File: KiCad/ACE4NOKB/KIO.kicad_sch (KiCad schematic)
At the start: 6 parts, among them J1 Conn_02x06_Odd_Even, J300 Conn_02x06_Odd_Even, J301 Conn_02x06_Odd_Even, J303 Conn_02x06_Odd_Even, J305 Conn_02x05_Odd_Even

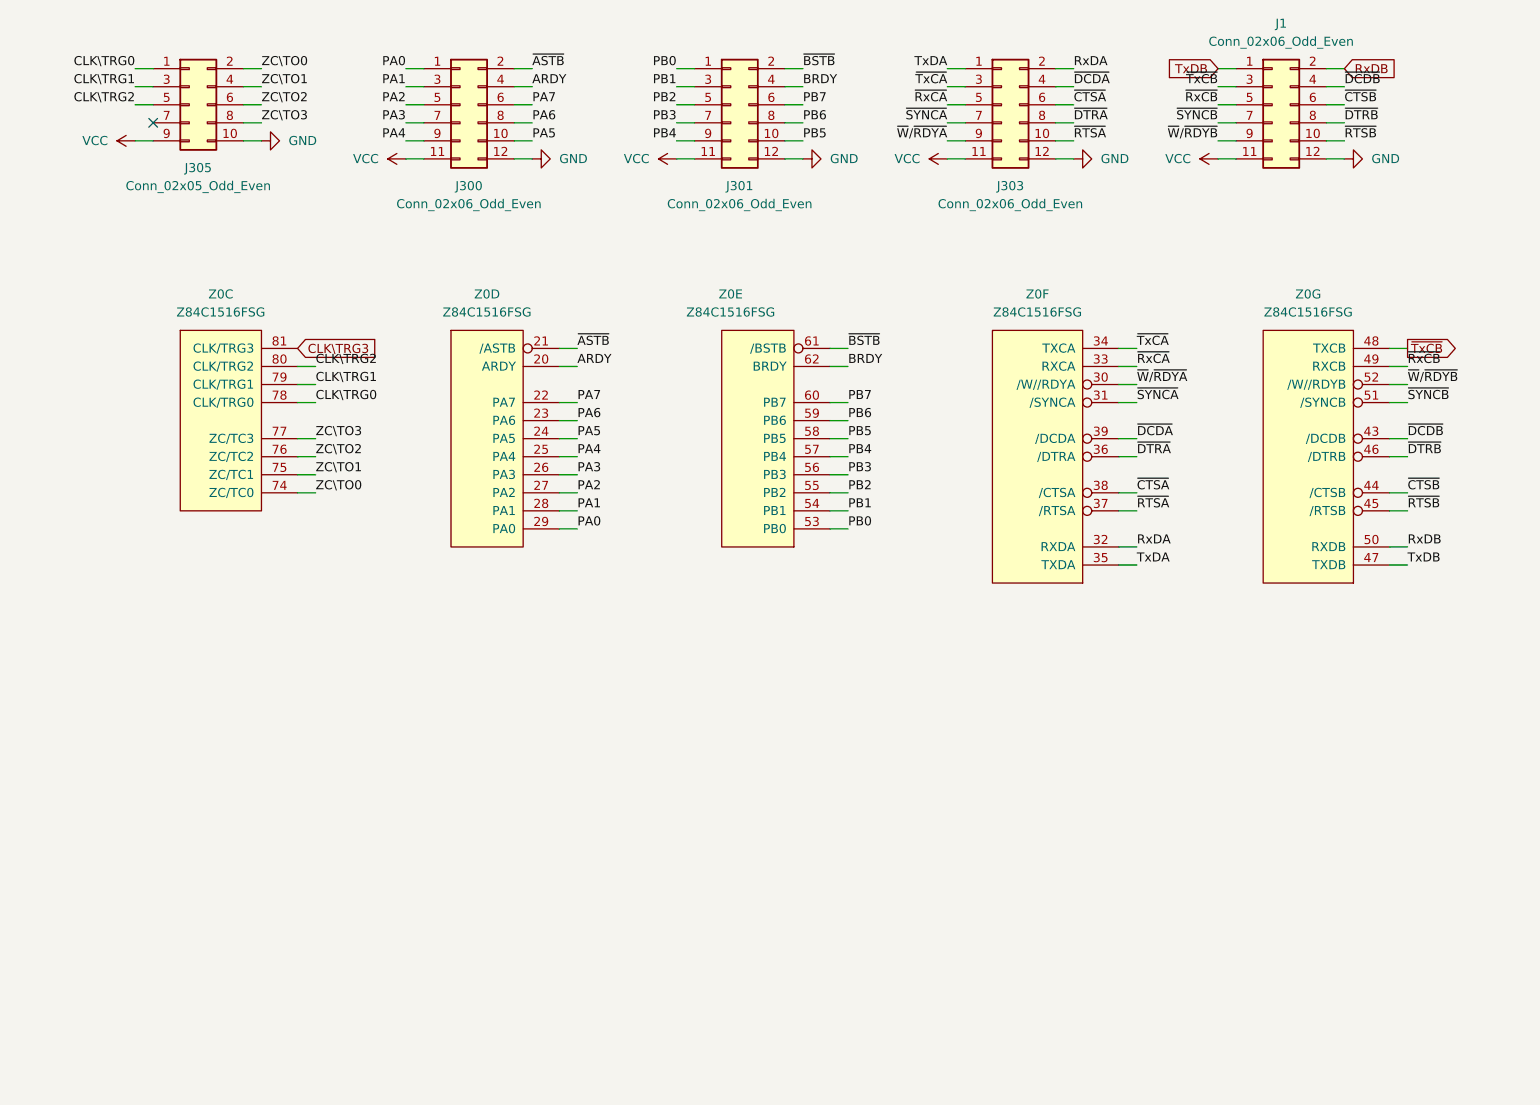
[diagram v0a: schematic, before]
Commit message: Fix mistake with ROM Select.
Signed-off-by: John Bradley <flypie@rocketmail.com>
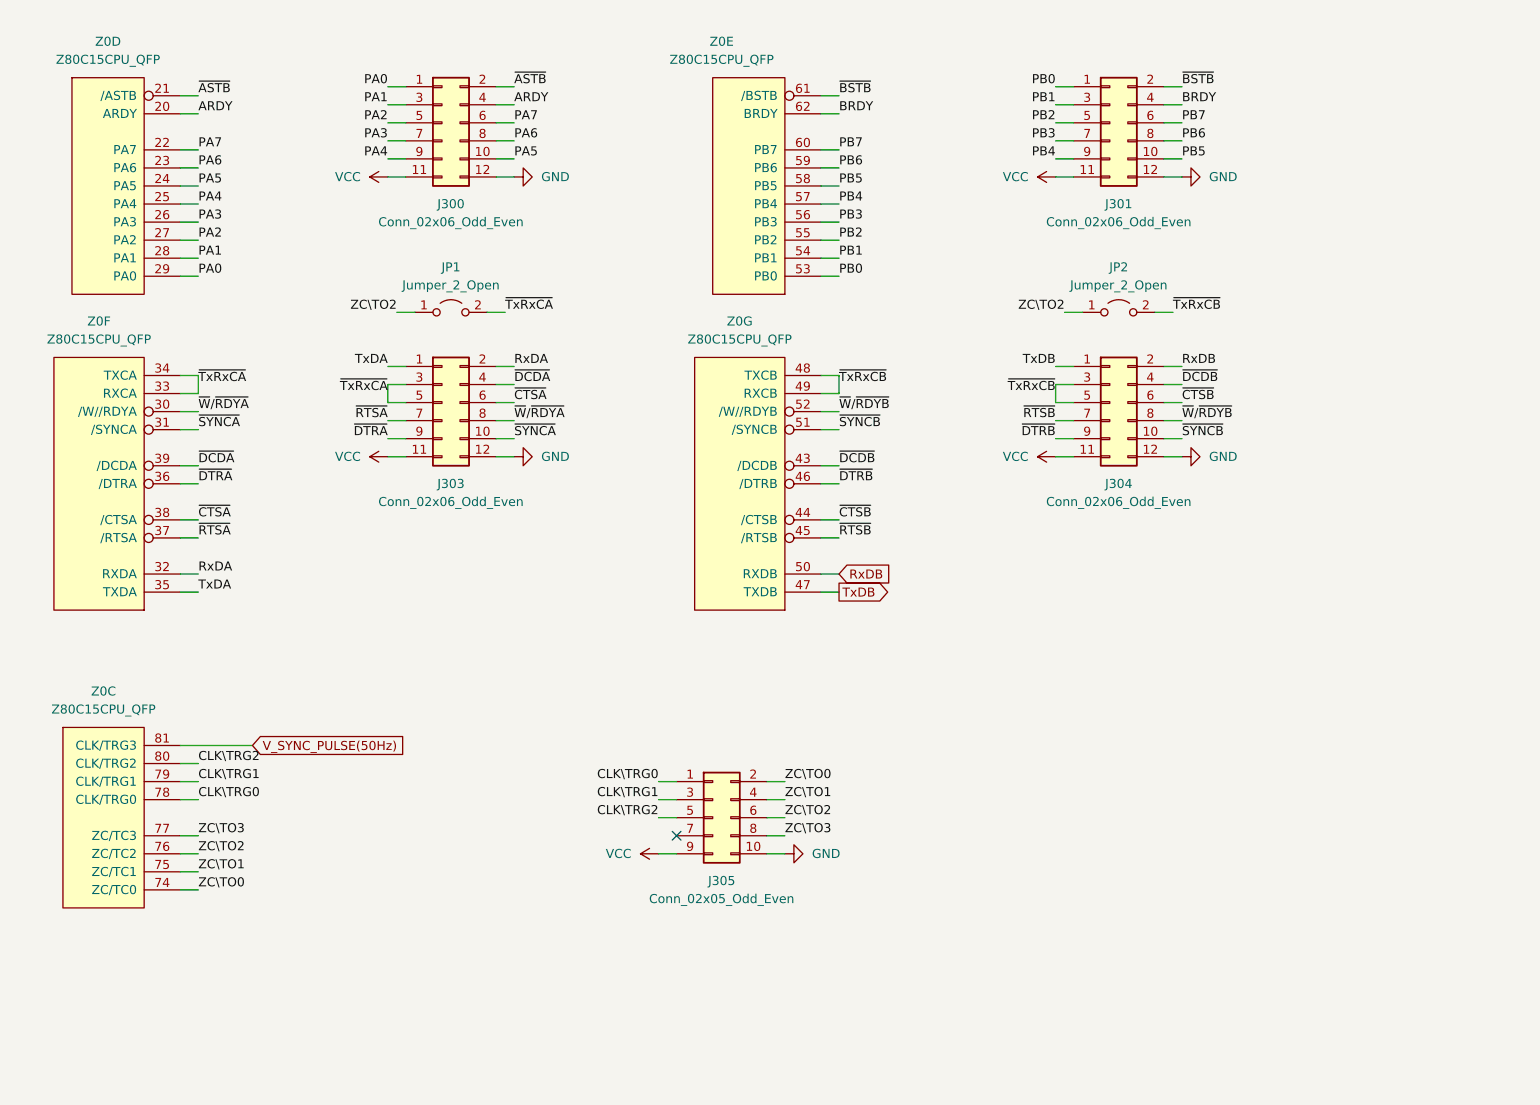
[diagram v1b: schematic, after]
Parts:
- removed J1: Conn_02x06_Odd_Even, Connector_PinHeader_2.54mm:PinHeader_2x06_P2.54mm_Vertical, symbol Connector_Generic:Conn_02x06_Odd_Even
- added J304: Conn_02x06_Odd_Even, Connector_PinHeader_2.54mm:PinHeader_2x06_P2.54mm_Vertical, symbol Connector_Generic:Conn_02x06_Odd_Even
- added JP1, JP2: Jumper_2_Open, Connector_PinHeader_2.54mm:PinHeader_1x02_P2.54mm_Vertical, symbol Jumper:Jumper_2_Open
- J300, J301: Manufacturer_Name Amphenol FCI -> SAMTEC; Manufacturer_Part_Number 10129381-912003BLF -> HTSW-106-08-S-D
- J303: Manufacturer_Name Amphenol FCI -> SAMTEC; Manufacturer_Part_Number 10129381-908002BLF -> TSW-104-08-S-D
- J305: Manufacturer_Name Amphenol FCI -> TE Connectivity / AMP; Manufacturer_Part_Number 10129381-910001BLF -> HTSW-105-08-S-D
- Z0: value Z84C1516FSG -> Z80C15CPU_QFP
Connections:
- net ~{TxCA} is gone; now on net ~{TxRxCA}: J303.3 (Pin_3), Z0.34 (TXCA)
- net ~{TxCB} is gone; now on net ~{TxRxCB}: Z0.48 (TXCB)
- net GND: now also J304.12 (Pin_12)
- net RxDB: now also J304.2 (Pin_2)
- net TxDB: now also J304.1 (Pin_1)
- net VCC: now also J304.11 (Pin_11)
- net ZC\TO2: now also JP1.1 (A), JP2.1 (A)
- net ~{CTSB}: now also J304.6 (Pin_6)
- net ~{DCDB}: now also J304.4 (Pin_4)
- net ~{DTRA}: now also J303.9 (Pin_9); no longer J303.8 (Pin_8)
- net ~{DTRB}: now also J304.9 (Pin_9)
- net ~{RTSA}: now also J303.7 (Pin_7); no longer J303.10 (Pin_10)
- net ~{RTSB}: now also J304.7 (Pin_7)
- net ~{SYNCA}: now also J303.10 (Pin_10); no longer J303.7 (Pin_7)
- net ~{SYNCB}: now also J304.10 (Pin_10)
- net ~{W}/~{RDYA}: now also J303.8 (Pin_8); no longer J303.9 (Pin_9)
- net ~{W}/~{RDYB}: now also J304.8 (Pin_8)
- net CLK\TRG3 renamed V_SYNC_PULSE(50Hz)
- net ~{RxCA} renamed ~{TxRxCA}
- net ~{TxRxCA}: now also JP1.2 (B)
- net ~{RxCB} renamed ~{TxRxCB}
- net ~{TxRxCB}: now also J304.3 (Pin_3), J304.5 (Pin_5), JP2.2 (B)
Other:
- moved on the sheet: J300, J301, J303, J305

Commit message: Update to last expermintal version. Uses clock sythsiser and can be switched between full ACE compatible and inhanced IO. Should be able to switch between multiple ROM images tosred on the same chip.
Signed-off-by: John Bradley <flypie@rocketmail.com>
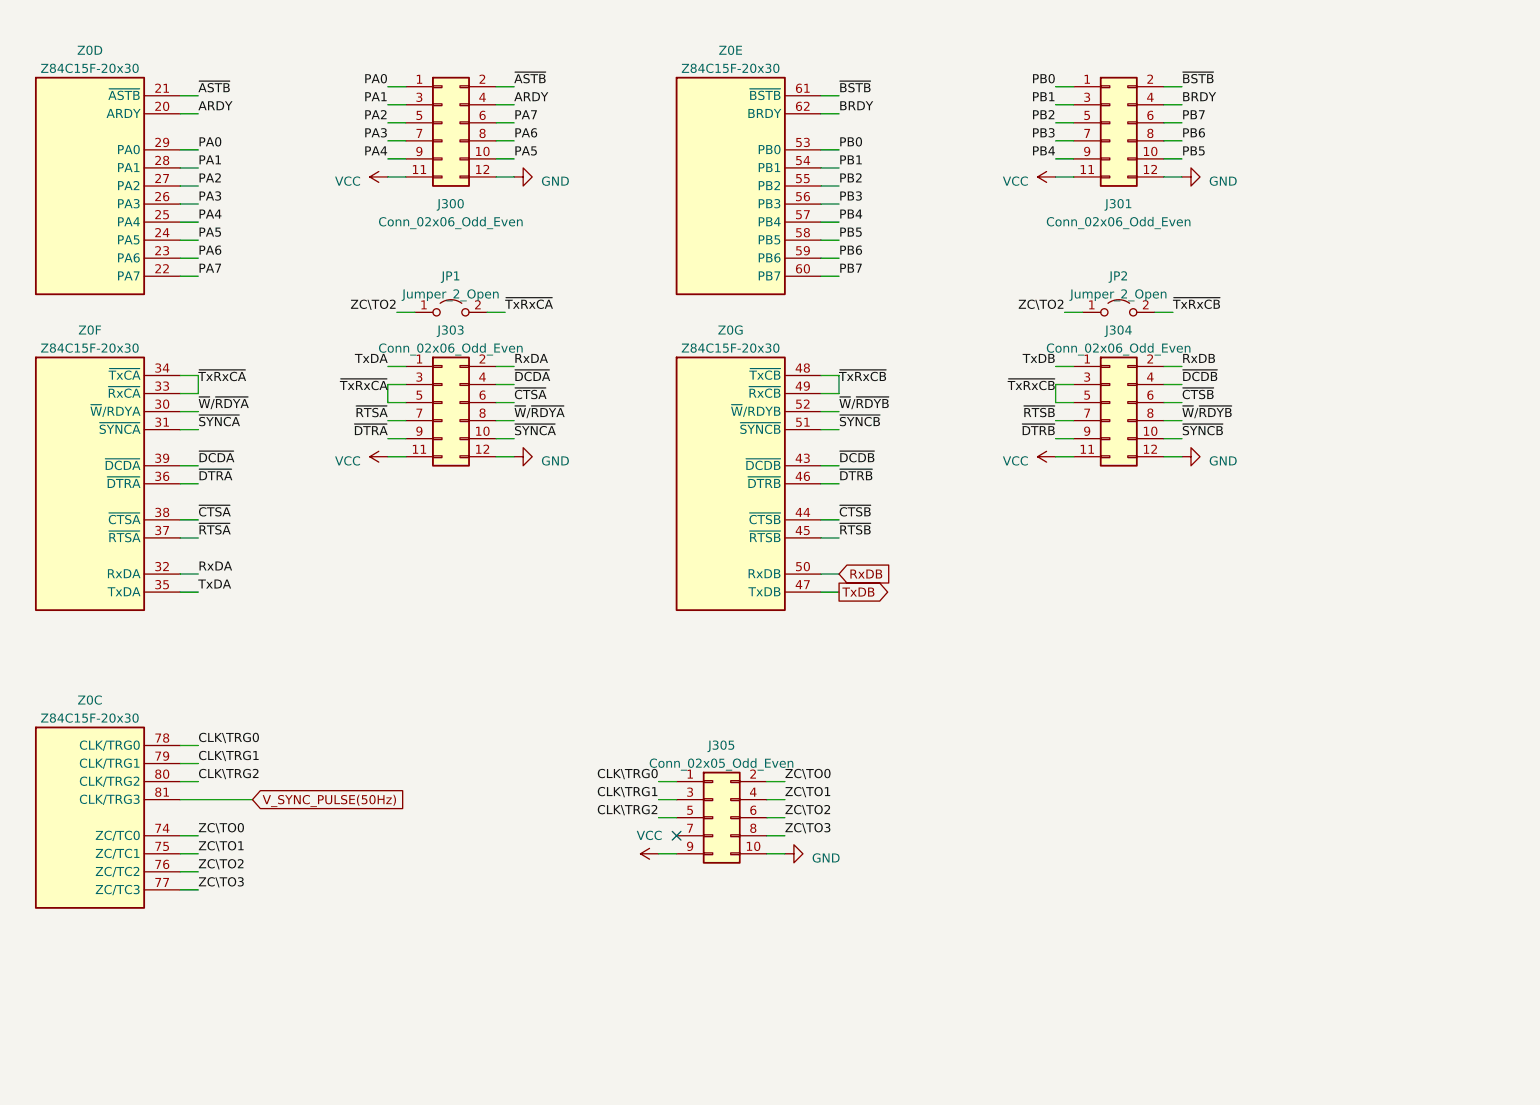
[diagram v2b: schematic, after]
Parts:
- J300, J301: Manufacturer_Name SAMTEC -> (none); Manufacturer_Part_Number HTSW-106-08-S-D -> (none)
- J303, J304: Manufacturer_Name SAMTEC -> (none); Manufacturer_Part_Number TSW-104-08-S-D -> (none)
- J305: Manufacturer_Name TE Connectivity / AMP -> (none); Manufacturer_Part_Number HTSW-105-08-S-D -> (none)
- Z0: value Z80C15CPU_QFP -> Z84C15F-20x30; symbol Zilog_Z80:Z84C15-QFP_ALT1 -> CPU_Zilog_Z80:Z84C15F-20x30; Manufacturer_Name Zilog -> (none); Manufacturer_Part_Number Z84C00 -> (none)
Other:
- moved on the sheet: Z0C

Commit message: Version with KIO replaced with Z84C15 and Video and Character RAM as MultiPorted.
Signed-off-by: John Bradley <flypie@rocketmail.com>
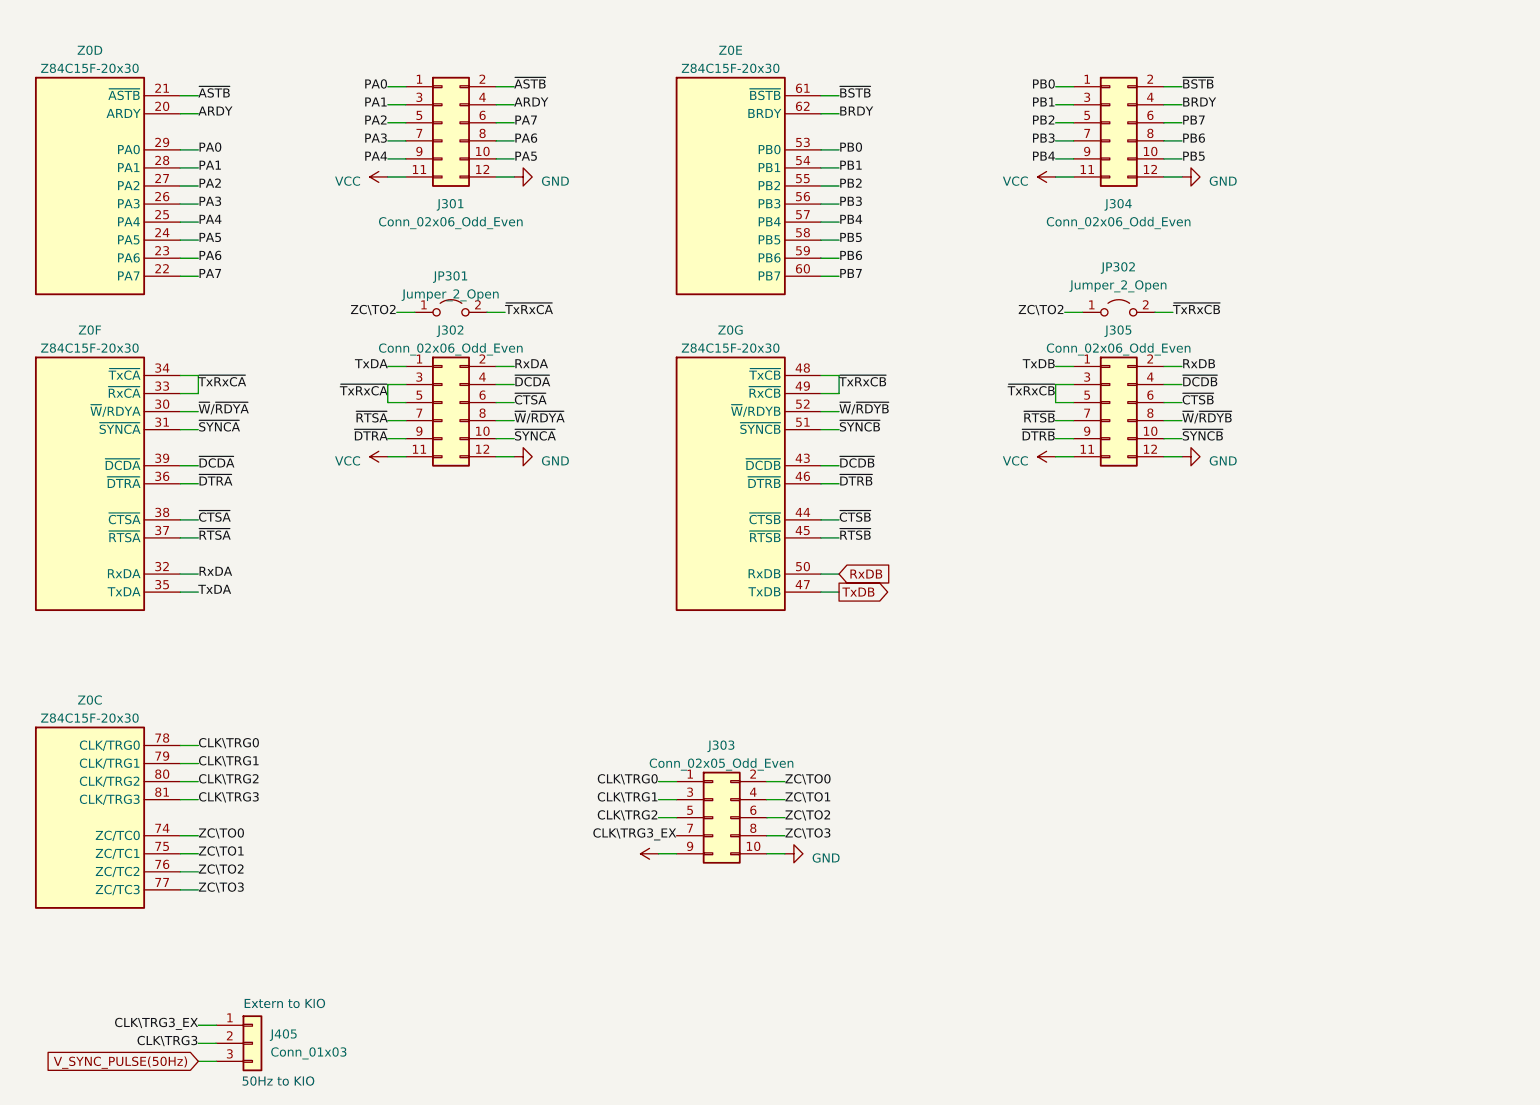
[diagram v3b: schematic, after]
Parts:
- added J405: Conn_01x03, Connector_PinHeader_2.54mm:PinHeader_1x03_P2.54mm_Vertical, symbol Connector_Generic:Conn_01x03
- renumbered J300 to J301, J303 to J302, J305 to J303, J301 to J304, J304 to J305, JP1 to JP301, JP2 to JP302
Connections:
- net V_SYNC_PULSE(50Hz): now also J405.3 (Pin_3); no longer Z0.81 (CLK/TRG3)
- net CLK\TRG3_EX: now reaches J303.7 (Pin_7)
- net CLK\TRG3_EX: now also J405.1 (Pin_1)
- new net CLK\TRG3: J405.2 (Pin_2), Z0.81 (CLK/TRG3)
- no-connect marks 1 -> 0
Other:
- note added: "50Hz to KIO"
- note added: "Extern to KIO"
